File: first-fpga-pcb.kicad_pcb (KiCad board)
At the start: 2 copper layers, 100 x 70 mm, 66 parts, among them J1 Conn_01x02, J2 Conn_01x08, J3 Conn_02x06_Top_Bottom, J4 Conn_02x06_Top_Bottom, J5 Conn_02x06_Top_Bottom, J6 Conn_02x06_Top_Bottom, J7 Conn_02x06_Top_Bottom, J8 Conn_02x06_Top_Bottom, SW1 SW_Push, SW2 SW_Push, U1 iCE40-HX1K-TQ144, U2 IS25LP016D-JBLE, U3 TLV73312PDBV, U4 TLV73333PDBV, X1 SiT2001B

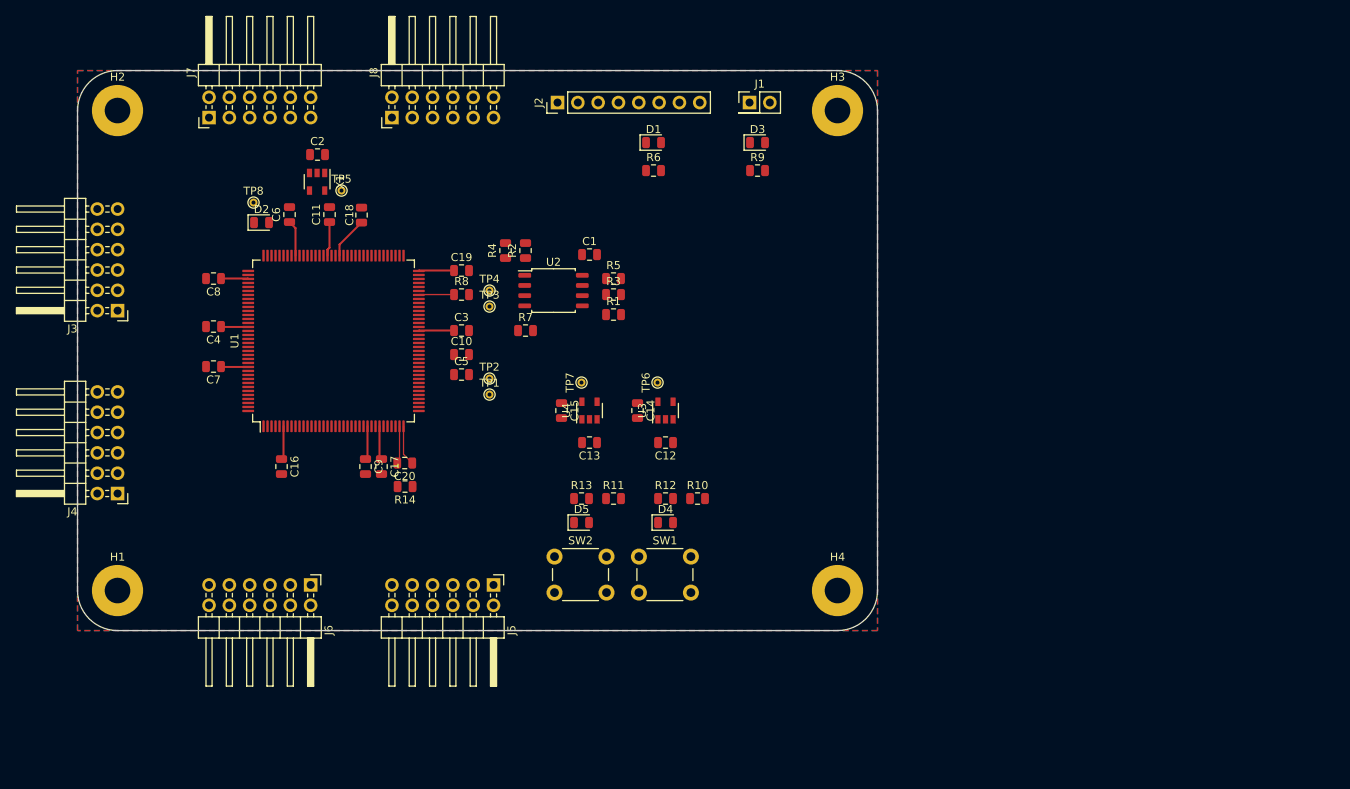
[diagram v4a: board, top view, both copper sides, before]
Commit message: change to 4k and finish routing
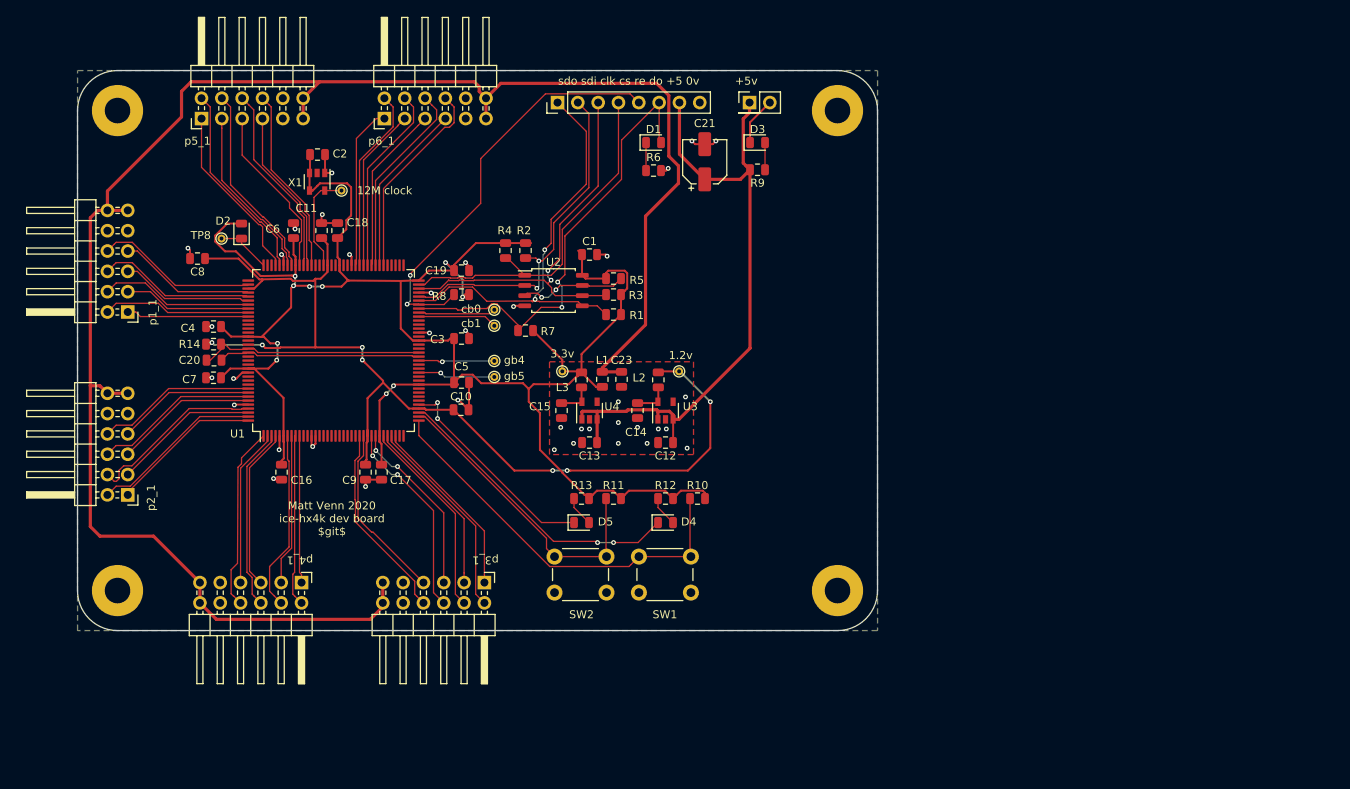
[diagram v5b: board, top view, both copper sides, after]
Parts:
- added C21: CP, Capacitor_SMD:CP_Elec_5x5.4, F.Cu at (153.4, 61.4)
- added C23: 100n, Capacitor_SMD:C_0805_2012Metric, F.Cu at (143.0, 88.6)
- added L1: L, Inductor_SMD:L_0805_2012Metric, F.Cu at (140.6, 88.6)
- added L2: L, Inductor_SMD:L_0805_2012Metric, F.Cu at (147.6, 88.7)
- added L3: L, Inductor_SMD:L_0805_2012Metric, F.Cu at (138.0, 88.7)
- J3, J4, J5, J6, J7, J8: value Conn_02x06_Top_Bottom -> Conn_02x06_Odd_Even
- U1: value iCE40-HX1K-TQ144 -> iCE40-HX4K-TQ144
- moved R14 29.8 mm to (92.0, 84.2)
- moved C20 27.1 mm to (92.1, 86.2), turned to 0 degrees
- moved C10 6.90 mm to (122.9, 92.4)
- moved TP8 6.02 mm to (93.0, 71.0)
- moved C18 3.57 mm to (107.5, 70.0)
- moved C8 3.20 mm to (90.0, 73.5)
- moved TP6 3.04 mm to (150.2, 87.6)
- moved TP7 2.78 mm to (135.6, 87.6)
- moved D2 2.72 mm to (95.5, 70.1), turned to 90 degrees
- moved TP3 2.47 mm to (127.1, 81.9)
- moved TP4 2.47 mm to (127.1, 79.9)
- moved TP1 2.28 mm to (127.1, 88.3)
- moved TP2 2.28 mm to (127.1, 86.3)
- moved C11 2.24 mm to (105.5, 70.0)
- moved C6 2.06 mm to (102.0, 70.0)
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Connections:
- C14 pad 1: +1V2 -> Net-(C14-Pad1)
- C15 pad 1: +3V3 -> Net-(C15-Pad1)
- J3 pad 10: /p1_10 -> GND
- J3 pad 11: GND -> +3.3VP
- J3 pad 12: +3V3 -> +3.3VP
- J3 pad 2: /p1_2 -> /p1_7
- J3 pad 3: /p1_3 -> /p1_2
- J3 pad 4: /p1_4 -> /p1_8
- J3 pad 5: GND -> /p1_3
- J3 pad 6: +3V3 -> /p1_9
- J3 pad 7: /p1_7 -> /p1_4
- J3 pad 8: /p1_8 -> /p1_10
- J3 pad 9: /p1_9 -> GND
- J4 pad 10: /p2_10 -> GND
- J4 pad 11: GND -> +3.3VP
- J4 pad 12: +3V3 -> +3.3VP
- J4 pad 2: /p2_2 -> /p2_7
- J4 pad 3: /p2_3 -> /p2_2
- J4 pad 4: /p2_4 -> /p2_8
- J4 pad 5: GND -> /p2_3
- J4 pad 6: +3V3 -> /p2_9
- J4 pad 7: /p2_7 -> /p2_4
- J4 pad 8: /p2_8 -> /p2_10
- J4 pad 9: /p2_9 -> GND
- J5 pad 10: /p3_10 -> GND
- J5 pad 11: GND -> +3.3VP
- J5 pad 12: +3V3 -> +3.3VP
- J5 pad 2: /p3_2 -> /p3_7
- J5 pad 3: /p3_3 -> /p3_2
- J5 pad 4: /p3_4 -> /p3_8
- J5 pad 5: GND -> /p3_3
- J5 pad 6: +3V3 -> /p3_9
- J5 pad 7: /p3_7 -> /p3_4
- J5 pad 8: /p3_8 -> /p3_10
- J5 pad 9: /p3_9 -> GND
- J6 pad 10: /p4_10 -> GND
- J6 pad 11: GND -> +3.3VP
- J6 pad 12: +3V3 -> +3.3VP
- J6 pad 2: /p4_2 -> /p4_7
- J6 pad 3: /p4_3 -> /p4_2
- J6 pad 4: /p4_4 -> /p4_8
- J6 pad 5: GND -> /p4_3
- J6 pad 6: +3V3 -> /p4_9
- J6 pad 7: /p4_7 -> /p4_4
- J6 pad 8: /p4_8 -> /p4_10
- J6 pad 9: /p4_9 -> GND
- J7 pad 10: /p5_10 -> GND
- J7 pad 11: GND -> +3.3VP
- J7 pad 12: +3V3 -> +3.3VP
- J7 pad 2: /p5_2 -> /p5_7
- J7 pad 3: /p5_3 -> /p5_2
- J7 pad 4: /p5_4 -> /p5_8
- J7 pad 5: GND -> /p5_3
- J7 pad 6: +3V3 -> /p5_9
- J7 pad 7: /p5_7 -> /p5_4
- J7 pad 8: /p5_8 -> /p5_10
- J7 pad 9: /p5_9 -> GND
- J8 pad 10: /p6_10 -> GND
- J8 pad 11: GND -> +3.3VP
- J8 pad 12: +3V3 -> +3.3VP
- J8 pad 2: /p6_2 -> /p6_7
- J8 pad 3: /p6_3 -> /p6_2
- J8 pad 4: /p6_4 -> /p6_8
- J8 pad 5: GND -> /p6_3
- J8 pad 6: +3V3 -> /p6_9
- J8 pad 7: /p6_7 -> /p6_4
- J8 pad 8: /p6_8 -> /p6_10
- J8 pad 9: /p6_9 -> GND
- U1 pad 101: /p5_2 -> /p5_8
- U1 pad 102: /p5_1 -> /p5_2
- U1 pad 104: Net-(U1-Pad104) -> /p5_7
- U1 pad 105: Net-(U1-Pad105) -> /p5_1
- U1 pad 11: /p3_10 -> Net-(U1-Pad11)
- U1 pad 110: Net-(U1-Pad110) -> /p1_10
- U1 pad 112: /p1_10 -> /p1_4
- U1 pad 114: /p1_8 -> /p1_3
- U1 pad 115: /p1_7 -> /p1_8
- U1 pad 116: /p1_4 -> /p1_2
- U1 pad 117: /p1_3 -> /p1_7
- U1 pad 118: /p1_2 -> /p1_1
- U1 pad 119: /p1_1 -> Net-(U1-Pad119)
- U1 pad 12: /p3_9 -> Net-(U1-Pad12)
- U1 pad 120: /p2_10 -> Net-(U1-Pad120)
- U1 pad 121: /p2_9 -> Net-(U1-Pad121)
- U1 pad 122: /p2_8 -> Net-(U1-Pad122)
- U1 pad 126: Net-(U1-Pad126) -> /vcc_pll
- U1 pad 127: Net-(U1-Pad127) -> Net-(C20-Pad2)
- U1 pad 128: /p2_7 -> Net-(U1-Pad128)
- U1 pad 129: /p2_4 -> Net-(U1-Pad129)
- U1 pad 131: Net-(U1-Pad131) -> +3V3
- U1 pad 133: +3V3 -> Net-(U1-Pad133)
- U1 pad 134: /p2_3 -> Net-(U1-Pad134)
- U1 pad 135: /p2_2 -> Net-(U1-Pad135)
- U1 pad 136: /p2_1 -> /p2_10
- U1 pad 137: Net-(U1-Pad137) -> /p2_4
- U1 pad 138: Net-(U1-Pad138) -> /p2_9
- U1 pad 139: Net-(U1-Pad139) -> /p2_3
- U1 pad 141: Net-(U1-Pad141) -> /p2_8
- U1 pad 142: Net-(U1-Pad142) -> /p2_2
- U1 pad 143: Net-(U1-Pad143) -> /p2_7
- U1 pad 144: Net-(U1-Pad144) -> /p2_1
- U1 pad 19: /p3_8 -> Net-(U1-Pad19)
- U1 pad 2: /p4_9 -> /p4_4
- U1 pad 20: /p3_7 -> Net-(U1-Pad20)
- U1 pad 21: /p3_4 -> Net-(U1-Pad21)
- U1 pad 22: /p3_3 -> Net-(U1-Pad22)
- U1 pad 23: /p3_2 -> Net-(U1-Pad23)
- U1 pad 24: /p3_1 -> Net-(U1-Pad24)
- U1 pad 25: Net-(U1-Pad25) -> /p3_10
- U1 pad 26: Net-(U1-Pad26) -> /p3_4
- U1 pad 28: Net-(U1-Pad28) -> /p3_9
- U1 pad 29: Net-(U1-Pad29) -> /p3_3
- U1 pad 3: /p4_8 -> /p4_9
- U1 pad 31: Net-(U1-Pad31) -> /p3_8
- U1 pad 32: Net-(U1-Pad32) -> /p3_2
- U1 pad 33: Net-(U1-Pad33) -> /p3_7
- U1 pad 34: Net-(U1-Pad34) -> /p3_1
- U1 pad 35: Net-(C20-Pad2) -> Net-(U1-Pad35)
- U1 pad 36: /vcc_pll -> Net-(U1-Pad36)
- U1 pad 37: Net-(U1-Pad37) -> /button1
- U1 pad 38: Net-(U1-Pad38) -> /button2
- U1 pad 39: Net-(U1-Pad39) -> /led1
- U1 pad 4: /p4_7 -> /p4_3
- U1 pad 40: Net-(U1-Pad40) -> +1V2
- U1 pad 41: Net-(U1-Pad41) -> /led2
- U1 pad 44: Net-(TP1-Pad1) -> Net-(U1-Pad44)
- U1 pad 45: Net-(TP2-Pad1) -> Net-(U1-Pad45)
- U1 pad 49: Net-(U1-Pad49) -> Net-(TP1-Pad1)
- U1 pad 51: +1V2 -> Net-(U1-Pad51)
- U1 pad 52: Net-(U1-Pad52) -> Net-(TP2-Pad1)
- U1 pad 53: Net-(U1-Pad53) -> Net-(C20-Pad2)
- U1 pad 54: Net-(U1-Pad54) -> /vcc_pll
- U1 pad 7: /p4_4 -> /p4_8
- U1 pad 73: /button1 -> Net-(U1-Pad73)
- U1 pad 74: /button2 -> Net-(U1-Pad74)
- U1 pad 75: /led1 -> Net-(U1-Pad75)
- U1 pad 76: /led2 -> Net-(U1-Pad76)
- U1 pad 79: /p6_9 -> /p6_4
- U1 pad 8: /p4_3 -> /p4_2
- U1 pad 80: /p6_8 -> /p6_9
- U1 pad 81: /p6_7 -> /p6_3
- U1 pad 82: Net-(U1-Pad82) -> /p6_8
- U1 pad 83: Net-(U1-Pad83) -> /p6_2
- U1 pad 84: Net-(U1-Pad84) -> /p6_7
- U1 pad 85: Net-(U1-Pad85) -> /p6_1
- U1 pad 87: /p6_4 -> Net-(U1-Pad87)
- U1 pad 88: /p6_3 -> Net-(U1-Pad88)
- U1 pad 9: /p4_2 -> /p4_7
- U1 pad 90: /p6_2 -> Net-(U1-Pad90)
- U1 pad 91: /p6_1 -> Net-(U1-Pad91)
- U1 pad 94: /p5_10 -> Net-(U1-Pad94)
- U1 pad 95: /p5_9 -> Net-(U1-Pad95)
- U1 pad 96: /p5_8 -> /p5_10
- U1 pad 97: /p5_7 -> /p5_4
- U1 pad 98: /p5_4 -> /p5_9
- U3 pad 5: +1V2 -> Net-(C14-Pad1)
- U4 pad 5: +3V3 -> Net-(C15-Pad1)
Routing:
- net +3.3VP: track 0.00 -> 227.4 mm
- net +3V3: track 33.9 -> 254.5 mm, vias 0 -> 10
- net +1V2: track 11.9 -> 130.5 mm, vias 0 -> 7
- net +5V: track 0.00 -> 82.9 mm
- net /cdone: track 0.00 -> 57.5 mm, vias 0 -> 2
- net /sdo: track 0.00 -> 54.8 mm, vias 0 -> 2
- net /sd_clk: track 0.00 -> 50.7 mm, vias 0 -> 2
- net /button1: track 0.00 -> 50.5 mm
- net GND: track 0.00 -> 49.5 mm, vias 0 -> 38
- net /creset: track 4.42 -> 52.0 mm, vias 0 -> 2
- net /sd_cs: track 0.00 -> 45.8 mm
- net /sdi: track 0.00 -> 44.2 mm, vias 0 -> 2
- net /button2: track 0.00 -> 38.7 mm
- net /led1: track 0.00 -> 37.7 mm, vias 0 -> 2
- net /led2: track 0.00 -> 26.9 mm, vias 0 -> 2
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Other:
- net class power5 added: clearance 0.16, trace_width 0.4, via_dia 1, via_drill 0.4
- board text added: "+5v"
- board text added: "1.2v"
- board text added: "12M clock"
- board text added: "3.3v"
- board text added: "Matt Venn 2020 ice-hx4k dev board $git$"
- board text added: "cb0"
- board text added: "cb1"
- board text added: "gb4"
- board text added: "gb5"
- board text added: "p1_1"
- board text added: "p2_1"
- board text added: "p3_1"
- board text added: "p4_1"
- board text added: "p5_1"
- board text added: "p6_1"
- board text added: "sdo sdi clk cs re do +5 0v"

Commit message: added raspi header, fattened psu traces, moved psu to top
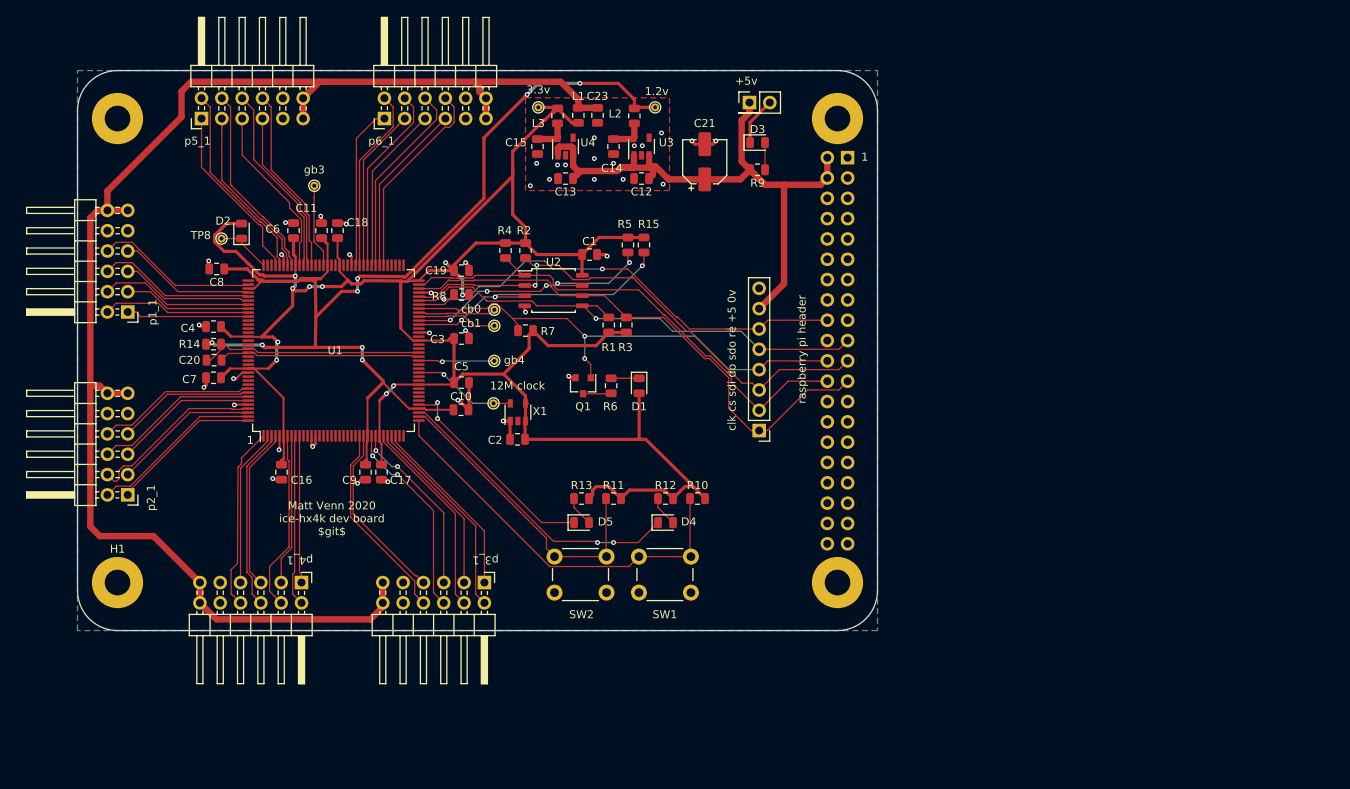
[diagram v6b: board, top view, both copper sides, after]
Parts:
- added J9: Conn_02x20_Odd_Even, Connector_PinHeader_2.54mm:PinHeader_2x20_P2.54mm_Vertical, B.Cu at (171.3, 60.9)
- added Q1: Q_NMOS_GSD, Package_TO_SOT_SMD:SOT-23, F.Cu at (138.2, 89.4)
- added R15: dnp, Resistor_SMD:R_0805_2012Metric, F.Cu at (145.8, 71.8)
- R5: value 10k -> dnp
- R7: value 2.2k -> dnp
- TP1: value gbin5 -> gbin3
- moved J2 48.1 mm to (160.2, 95.0), turned to 180 degrees
- moved C2 43.5 mm to (130.0, 96.1), turned to 180 degrees
- moved X1 38.2 mm to (130.1, 92.7), turned to 90 degrees
- moved C12 33.1 mm to (145.5, 63.5)
- moved C13 33.1 mm to (136.0, 63.5)
- moved C14 33.1 mm to (142.0, 59.5)
- moved C15 33.1 mm to (132.5, 59.5)
- moved U3 33.1 mm to (145.5, 59.5)
- moved U4 33.1 mm to (136.0, 59.5)
- moved C23 33.1 mm to (140.0, 55.6)
- moved L1 33.1 mm to (137.6, 55.6)
- moved L2 33.1 mm to (144.6, 55.7)
- moved L3 33.1 mm to (135.0, 55.7)
- moved TP6 33.1 mm to (147.2, 54.6)
- moved TP7 33.1 mm to (132.6, 54.6)
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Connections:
- net Net-(C14-Pad1) renamed /1v2
- net Net-(C15-Pad1) renamed /3v3
- D1 pad 2: /cdone -> +3V3
- J2 pad 1: /sdo -> /sd_clk
- J2 pad 2: /sdi -> /sd_cs
- J2 pad 3: /sd_clk -> /sdi
- J2 pad 4: /sd_cs -> /cdone
- J2 pad 5: /creset -> /sdo
- J2 pad 6: /cdone -> /creset
- R5 pad 1: +3V3 -> /sd_io3
- R5 pad 2: Net-(R5-Pad2) -> +3V3
- R6 pad 2: GND -> Net-(Q1-Pad3)
- U1 pad 49: Net-(TP1-Pad1) -> /clock
- U1 pad 61: Net-(U1-Pad61) -> /sd_io2
- U1 pad 62: Net-(U1-Pad62) -> /sd_io3
- U1 pad 93: /clock -> Net-(TP1-Pad1)
- U2 pad 3: Net-(R5-Pad2) -> /sd_io2
- U2 pad 7: Net-(R5-Pad2) -> /sd_io3
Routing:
- net +3.3VP: track 227.4 -> 181.6 mm
- net +3V3: track 254.5 -> 297.6 mm
- net /sd_io2: track 0.00 -> 36.1 mm, vias 0 -> 3
- net /sd_io3: track 0.00 -> 33.9 mm, vias 0 -> 5
- net +1V2: track 130.5 -> 153.6 mm, vias 7 -> 8
- net /sdi: track 44.2 -> 66.7 mm
- net /sd_cs: track 45.8 -> 64.3 mm
- net /sd_clk: track 50.7 -> 67.1 mm, vias 2 -> 0
- net Net-(R5-Pad2): track 13.4 -> 0.00 mm, vias 2 -> 0
- net /creset: track 52.0 -> 61.5 mm
- net /sdo: track 54.8 -> 61.9 mm, vias 2 -> 1
- net +5V: track 82.9 -> 76.1 mm
- net /cdone: track 57.5 -> 61.8 mm
- net Net-(Q1-Pad3): track 0.00 -> 3.53 mm
- net GND: track 49.5 -> 47.3 mm, vias 38 -> 40
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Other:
- net class power: trace_width 0.25 -> 0.4
- net class power5: trace_width 0.4 -> 0.8
- board text added: "1"
- board text added: "clk cs sdi do sdo re +5 0v"
- board text added: "gb3"
- board text added: "raspberry pi header"
- board text removed: "gb5"
- board text removed: "sdo sdi clk cs re do +5 0v"

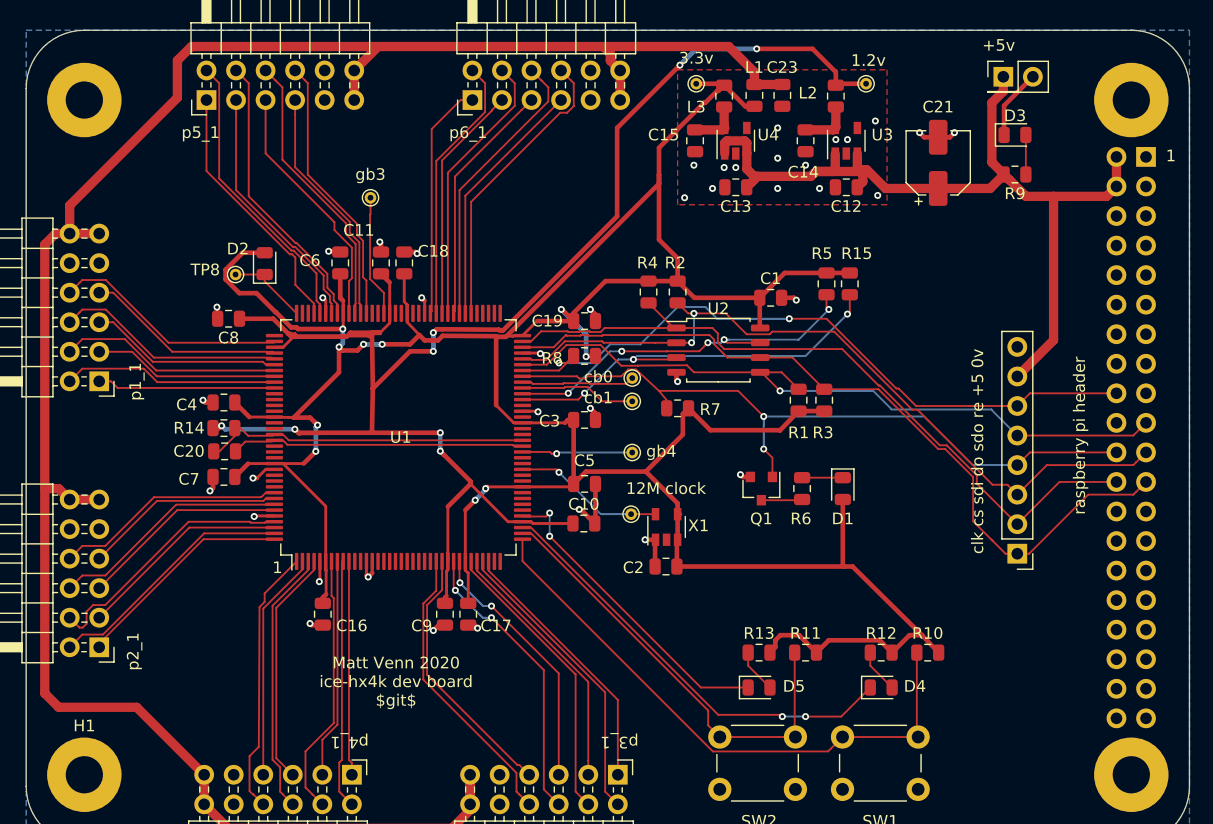
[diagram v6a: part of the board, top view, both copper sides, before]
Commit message: changed flash orientation for better routing, fixed upside down header
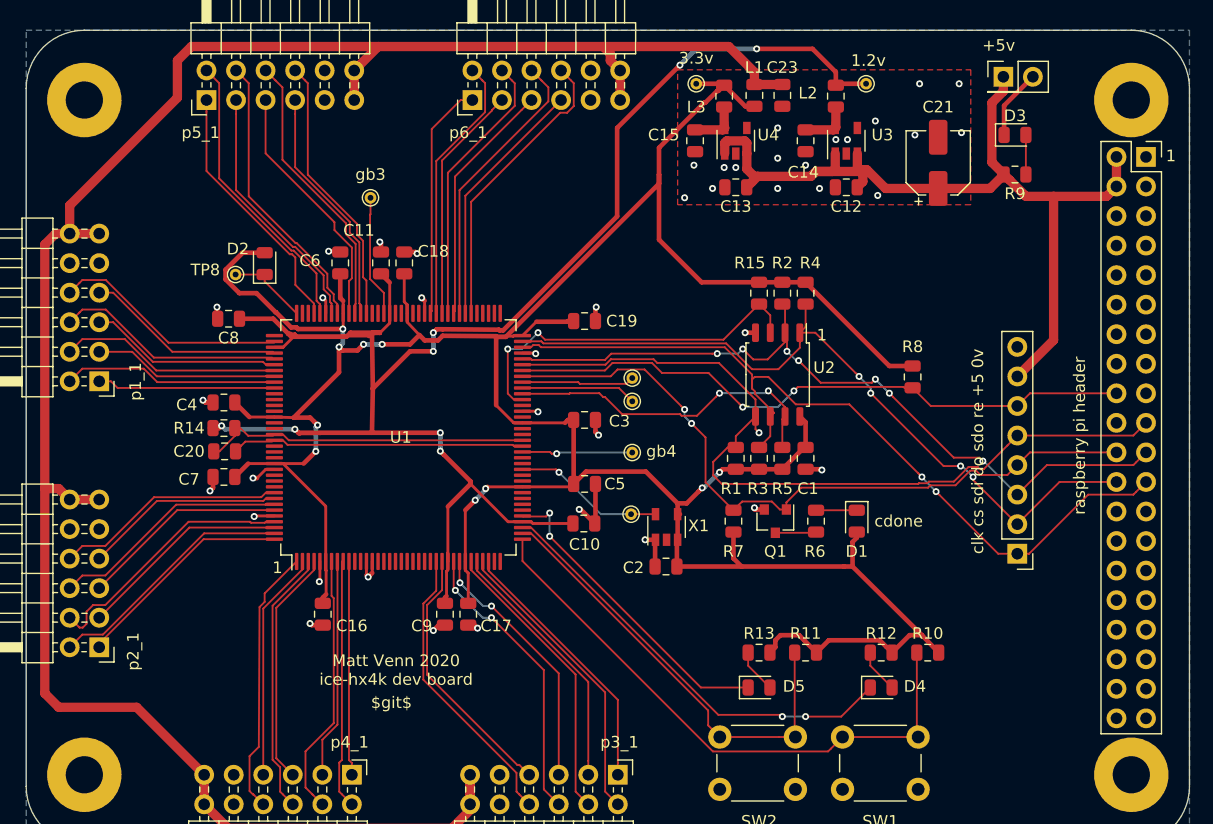
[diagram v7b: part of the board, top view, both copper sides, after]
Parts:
- J9: footprint Connector_PinHeader_2.54mm:PinHeader_2x20_P2.54mm_Vertical -> Connector_PinSocket_2.54mm:PinSocket_2x20_P2.54mm_Vertical; moved to F.Cu
- moved R8 28.3 mm to (151.2, 79.8), turned to 90 degrees
- moved R5 15.5 mm to (140.0, 86.8), turned to 270 degrees
- moved C1 14.1 mm to (142.0, 86.8), turned to 270 degrees
- moved R4 13.5 mm to (142.0, 72.6)
- moved R7 10.8 mm to (135.8, 92.2), turned to 270 degrees
- moved R2 9.00 mm to (140.0, 72.6)
- moved R15 7.84 mm to (138.0, 72.6)
- moved R3 7.51 mm to (138.0, 86.8)
- moved R1 7.36 mm to (136.0, 86.8)
- moved U2 5.52 mm to (139.6, 79.6), turned to 270 degrees
- moved D1 3.05 mm to (146.4, 92.2)
- moved Q1 3.05 mm to (139.4, 92.2)
- moved R6 3.05 mm to (142.9, 92.2)
- turned J9 to 0 degrees
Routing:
- net +3V3: track 297.6 -> 279.1 mm
- net /sdo: track 61.9 -> 71.5 mm
- net /creset: track 61.5 -> 54.8 mm
- net /sd_io3: track 33.9 -> 28.4 mm, vias 5 -> 2
- net /sd_clk: track 67.1 -> 72.0 mm, vias 0 -> 2
- net /sd_io2: track 36.1 -> 31.9 mm, vias 3 -> 2
- net GND: track 47.3 -> 44.0 mm, vias 40 -> 42
- net /sd_cs: track 64.3 -> 65.5 mm, vias 0 -> 4
- net /sdi: vias 2 -> 7
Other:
- board text added: "$git$"
- board text added: "Matt Venn 2020 ice-hx4k dev board"
- board text added: "cdone"
- board text removed: "12M clock"
- board text removed: "Matt Venn 2020 ice-hx4k dev board $git$"
- board text removed: "cb0"
- board text removed: "cb1"
